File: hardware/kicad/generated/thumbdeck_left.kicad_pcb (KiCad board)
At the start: 2 copper layers, 63 x 107.9 mm, 0 parts

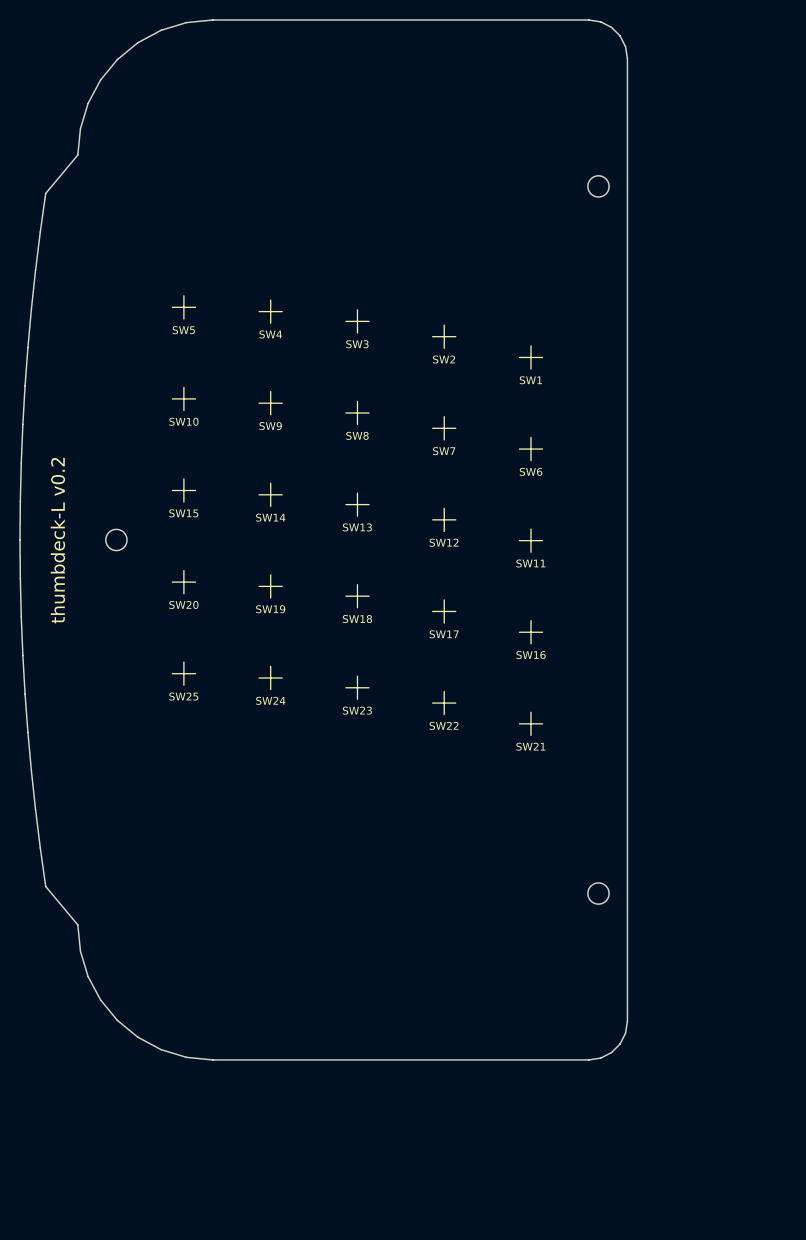
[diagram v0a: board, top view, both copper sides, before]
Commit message: hardware(v0.3): role-based geometry, grader, board gen
- deck.py: right grip = mcu (nice!nano/LiPo/USB-C/bridge), left = passive matrix
  + bridge connector; symmetric outline, mirrored key field
- grade.py: 17 checks incl. F-bridge + F-role; nice!nano pro_micro pin validity;
  single 5x10 transform (dropped split-specific checks)
- gen_kicad/render_fab/matrix_map updated for single controller

Co-Authored-By: Claude Opus 4.8 (1M context) <noreply@anthropic.com>
Claude-Session: https://claude.ai/code/session_01AmPvvwwHX98PjdDnPxhX97
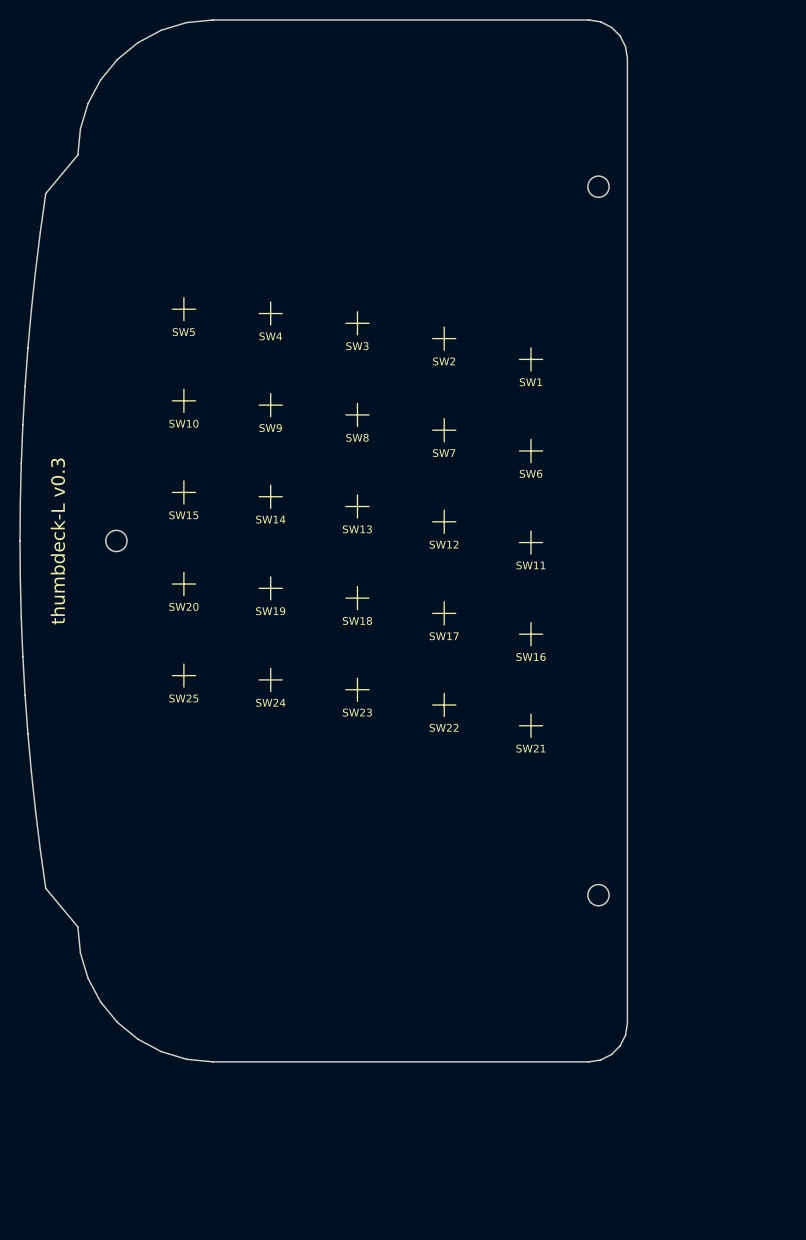
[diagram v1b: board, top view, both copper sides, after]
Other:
- board size 63 x 107.9 mm -> 63 x 108.1 mm
- board text added: "BRIDGE"
- board text added: "thumbdeck-L v0.3"
- board text removed: "CONTROLLER"
- board text removed: "LIPO"
- board text removed: "USB-C"
- board text removed: "thumbdeck-L v0.2"

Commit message: v0.4: encode EE design review into the grade, re-converge to PASS
Turn the professional EE review findings into enforced checks and fix the design
to satisfy them (functional 27/27, visual 9/9, OVERALL PASS).

Geometry/RF:
- nice!nano remounted vertical at top; nRF52840 ANTENNA keep-out overhangs the
  top edge (no copper under RF path), LiPo kept ~90mm away; USB in an access gap
- new hard check F-antenna; F-role now requires antenna on right / passive left

Bridge signal integrity:
- kscan debounce 8ms (F-si-debounce); BOM adds 4.7k row pull-downs, 100-330R
  column series R, TVS, shielded flex (F-si-passives, F-esd-tvs)

Process/plan gates (now graded):
- F-charge (1C vs cell), F-switch-verify (meter pinout), F-review-doc
  (docs/design-review.md + FMEA), F-bringup (current-draw checkpoints),
  F-fab-gates (README gates fab on schematic+ERC+DRC+CI)

Fixes: antenna/controller touching edge tripped float overlap -> 0.6mm gap;
BOM 'series res' substring broke on markdown bold -> looser check.
Bump VERSION v0.3 -> v0.4; regenerate all renders/board/soldermap.

Co-Authored-By: Claude Opus 4.8 (1M context) <noreply@anthropic.com>
Claude-Session: https://claude.ai/code/session_01AmPvvwwHX98PjdDnPxhX97
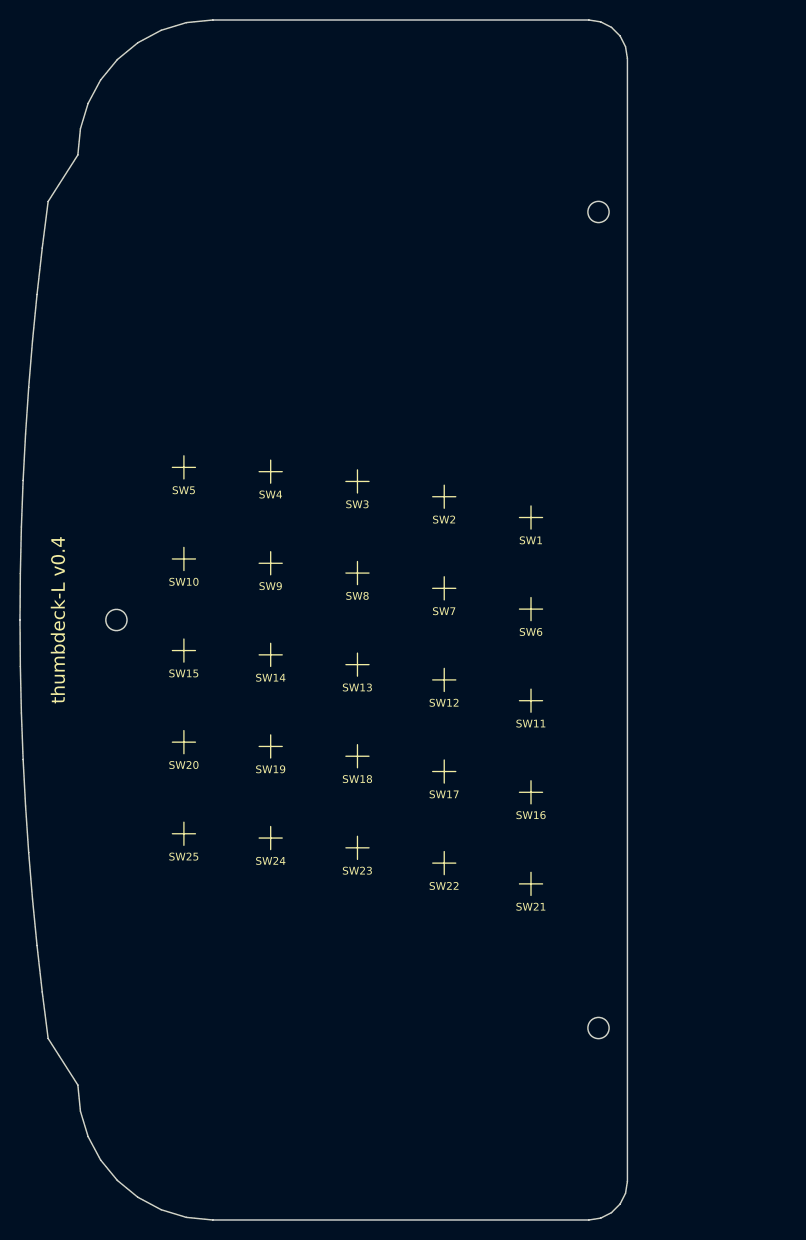
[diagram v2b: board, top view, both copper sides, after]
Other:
- board size 63 x 108.1 mm -> 63 x 124.5 mm
- board text added: "thumbdeck-L v0.4"
- board text removed: "thumbdeck-L v0.3"

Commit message: v0.12: snap-dome phone MagSafe deck — module, turnkey PCBA, stackable layer renders
Redesign from v0.4 (50-key nice!nano) to a landscape-phone MagSafe deck:

- Switches: Snaptron 7mm snap domes on a one-piece 3D-printed living-hinge keymat
  (PocketMage-style); footprint extracted to hardware/footprints/. 81 keys (2x 6x6
  grids + D-pad/OK + mouse + PgUp/Dn), digitized from the sketch to
  hardware/layout/keymat.json.
- Form: phone landscape, MagSafe-mounted centre; LiPo in the spine behind the ring;
  two ~70x102mm grips clamped to the outline; PCB-integrated trackpad (Azoteq IQS7211E).
- Electronics (5-lens EE/PD review): one Ebyte E73 nRF52840 module, 9x10 col2row
  matrix with SOD-323 diodes on the back, power front-end (MCP73831/USB-C+CC/ESD),
  vertical JST-GH bridge, ENIG. Layer-correct traces (cols front / rows back / vias),
  PCB meander antenna option.
- Sourcing (JLC vs PCBWay review): JLCPCB single-sided turnkey, ~$150-230/5 sets;
  part swaps + LCSC part numbers in docs/fabrication-sourcing.md.
- Real netlisted KiCad boards via pcbnew (gen_kicad_pcbnew.py) + front/back SVGs.
- 5 stackable layer renders (render_layers.py) + product/fab views; README rewritten.
- Cleanup: old 50-key loop scripts -> hardware/scripts/legacy/; old iters/renders
  -> renders/history/.

Co-Authored-By: Claude Opus 4.8 <noreply@anthropic.com>
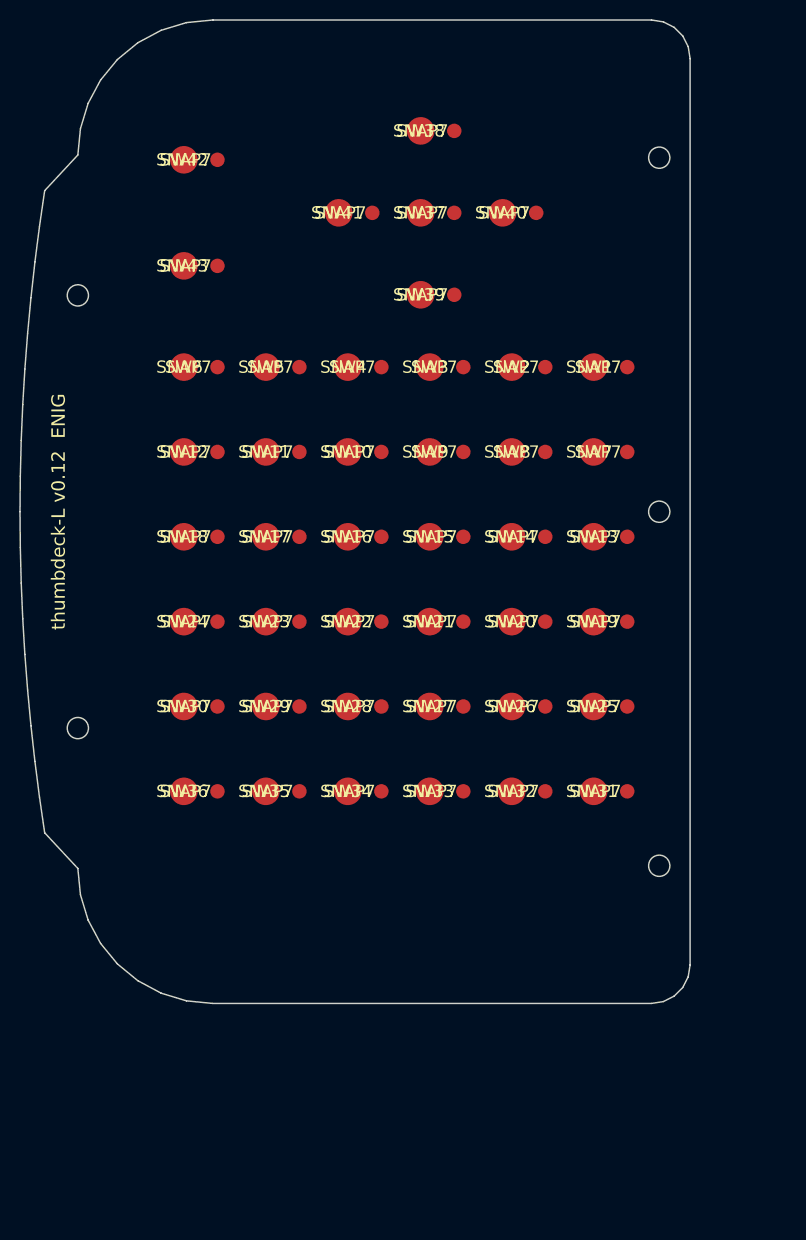
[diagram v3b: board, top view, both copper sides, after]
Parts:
- added D1: 1N4148WS, D_SOD-323, B.Cu at (59.5, 35.8)
- added D10: 1N4148WS, D_SOD-323, B.Cu at (34.0, 44.6)
- added D11: 1N4148WS, D_SOD-323, B.Cu at (25.5, 44.6)
- added D12: 1N4148WS, D_SOD-323, B.Cu at (17.0, 44.6)
- added D13: 1N4148WS, D_SOD-323, B.Cu at (59.5, 53.4)
- added D14: 1N4148WS, D_SOD-323, B.Cu at (51.0, 53.4)
- added D15: 1N4148WS, D_SOD-323, B.Cu at (42.5, 53.4)
- added D16: 1N4148WS, D_SOD-323, B.Cu at (34.0, 53.4)
- added D17: 1N4148WS, D_SOD-323, B.Cu at (25.5, 53.4)
- added D18: 1N4148WS, D_SOD-323, B.Cu at (17.0, 53.4)
- added D19: 1N4148WS, D_SOD-323, B.Cu at (59.5, 62.2)
- added D2: 1N4148WS, D_SOD-323, B.Cu at (51.0, 35.8)
- added D20: 1N4148WS, D_SOD-323, B.Cu at (51.0, 62.2)
- added D21: 1N4148WS, D_SOD-323, B.Cu at (42.5, 62.2)
- added D22: 1N4148WS, D_SOD-323, B.Cu at (34.0, 62.2)
- added D23: 1N4148WS, D_SOD-323, B.Cu at (25.5, 62.2)
- added D24: 1N4148WS, D_SOD-323, B.Cu at (17.0, 62.2)
- added D25: 1N4148WS, D_SOD-323, B.Cu at (59.5, 71.0)
- added D26: 1N4148WS, D_SOD-323, B.Cu at (51.0, 71.0)
- added D27: 1N4148WS, D_SOD-323, B.Cu at (42.5, 71.0)
- added D28: 1N4148WS, D_SOD-323, B.Cu at (34.0, 71.0)
- added D29: 1N4148WS, D_SOD-323, B.Cu at (25.5, 71.0)
- added D3: 1N4148WS, D_SOD-323, B.Cu at (42.5, 35.8)
- added D30: 1N4148WS, D_SOD-323, B.Cu at (17.0, 71.0)
- added D31: 1N4148WS, D_SOD-323, B.Cu at (59.5, 79.8)
- added D32: 1N4148WS, D_SOD-323, B.Cu at (51.0, 79.8)
- added D33: 1N4148WS, D_SOD-323, B.Cu at (42.5, 79.8)
- added D34: 1N4148WS, D_SOD-323, B.Cu at (34.0, 79.8)
- added D35: 1N4148WS, D_SOD-323, B.Cu at (25.5, 79.8)
- added D36: 1N4148WS, D_SOD-323, B.Cu at (17.0, 79.8)
- added D37: 1N4148WS, D_SOD-323, B.Cu at (41.6, 19.8)
- added D38: 1N4148WS, D_SOD-323, B.Cu at (41.6, 11.3)
- added D39: 1N4148WS, D_SOD-323, B.Cu at (41.6, 28.3)
- added D4: 1N4148WS, D_SOD-323, B.Cu at (34.0, 35.8)
- added D40: 1N4148WS, D_SOD-323, B.Cu at (50.1, 19.8)
- added D41: 1N4148WS, D_SOD-323, B.Cu at (33.1, 19.8)
- added D42: 1N4148WS, D_SOD-323, B.Cu at (17.0, 14.3)
- added D43: 1N4148WS, D_SOD-323, B.Cu at (17.0, 25.3)
- added D5: 1N4148WS, D_SOD-323, B.Cu at (25.5, 35.8)
- added D6: 1N4148WS, D_SOD-323, B.Cu at (17.0, 35.8)
- added D7: 1N4148WS, D_SOD-323, B.Cu at (59.5, 44.6)
- added D8: 1N4148WS, D_SOD-323, B.Cu at (51.0, 44.6)
- added D9: 1N4148WS, D_SOD-323, B.Cu at (42.5, 44.6)
- added SW1: SNAP7, , F.Cu at (59.5, 36.0)
- added SW10: SNAP7, , F.Cu at (34.0, 44.8)
- added SW11: SNAP7, , F.Cu at (25.5, 44.8)
- added SW12: SNAP7, , F.Cu at (17.0, 44.8)
- added SW13: SNAP7, , F.Cu at (59.5, 53.6)
- added SW14: SNAP7, , F.Cu at (51.0, 53.6)
- added SW15: SNAP7, , F.Cu at (42.5, 53.6)
- added SW16: SNAP7, , F.Cu at (34.0, 53.6)
- added SW17: SNAP7, , F.Cu at (25.5, 53.6)
- added SW18: SNAP7, , F.Cu at (17.0, 53.6)
- added SW19: SNAP7, , F.Cu at (59.5, 62.4)
- added SW2: SNAP7, , F.Cu at (51.0, 36.0)
- added SW20: SNAP7, , F.Cu at (51.0, 62.4)
- added SW21: SNAP7, , F.Cu at (42.5, 62.4)
- added SW22: SNAP7, , F.Cu at (34.0, 62.4)
- added SW23: SNAP7, , F.Cu at (25.5, 62.4)
- added SW24: SNAP7, , F.Cu at (17.0, 62.4)
- added SW25: SNAP7, , F.Cu at (59.5, 71.2)
- added SW26: SNAP7, , F.Cu at (51.0, 71.2)
- added SW27: SNAP7, , F.Cu at (42.5, 71.2)
- added SW28: SNAP7, , F.Cu at (34.0, 71.2)
- added SW29: SNAP7, , F.Cu at (25.5, 71.2)
- added SW3: SNAP7, , F.Cu at (42.5, 36.0)
- added SW30: SNAP7, , F.Cu at (17.0, 71.2)
- added SW31: SNAP7, , F.Cu at (59.5, 80.0)
- added SW32: SNAP7, , F.Cu at (51.0, 80.0)
- added SW33: SNAP7, , F.Cu at (42.5, 80.0)
- added SW34: SNAP7, , F.Cu at (34.0, 80.0)
- added SW35: SNAP7, , F.Cu at (25.5, 80.0)
- added SW36: SNAP7, , F.Cu at (17.0, 80.0)
- added SW37: SNAP7, , F.Cu at (41.6, 20.0)
- added SW38: SNAP7, , F.Cu at (41.6, 11.5)
- added SW39: SNAP7, , F.Cu at (41.6, 28.5)
- added SW4: SNAP7, , F.Cu at (34.0, 36.0)
- added SW40: SNAP7, , F.Cu at (50.1, 20.0)
- added SW41: SNAP7, , F.Cu at (33.1, 20.0)
- added SW42: SNAP7, , F.Cu at (17.0, 14.5)
- added SW43: SNAP7, , F.Cu at (17.0, 25.5)
- added SW5: SNAP7, , F.Cu at (25.5, 36.0)
- added SW6: SNAP7, , F.Cu at (17.0, 36.0)
- added SW7: SNAP7, , F.Cu at (59.5, 44.8)
- added SW8: SNAP7, , F.Cu at (51.0, 44.8)
- added SW9: SNAP7, , F.Cu at (42.5, 44.8)
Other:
- board size 63 x 124.5 mm -> 69.5 x 102 mm
- board text added: "ROUTING + MODULE/CONN FOOTPRINTS = NEXT GATE"
- board text added: "thumbdeck-L v0.12 ENIG"
- board text removed: "D1"
- board text removed: "D10"
- board text removed: "D11"
- board text removed: "D12"
- board text removed: "D13"
- board text removed: "D14"
- board text removed: "D15"
- board text removed: "D16"
- board text removed: "D17"
- board text removed: "D18"
- board text removed: "D19"
- board text removed: "D2"
- board text removed: "D20"
- board text removed: "D21"
- board text removed: "D22"
- board text removed: "D23"
- board text removed: "D24"
- board text removed: "D25"
- board text removed: "D3"
- board text removed: "D4"
- board text removed: "D5"
- board text removed: "D6"
- board text removed: "D7"
- board text removed: "D8"
- board text removed: "D9"
- board text removed: "SW1"
- board text removed: "SW10"
- board text removed: "SW11"
- board text removed: "SW12"
- board text removed: "SW13"
- board text removed: "SW14"
- board text removed: "SW15"
- board text removed: "SW16"
- board text removed: "SW17"
- board text removed: "SW18"
- board text removed: "SW19"
- board text removed: "SW2"
- board text removed: "SW20"
- board text removed: "SW21"
- board text removed: "SW22"
- board text removed: "SW23"
- board text removed: "SW24"
- board text removed: "SW25"
- board text removed: "SW3"
- board text removed: "SW4"
- board text removed: "SW5"
- board text removed: "SW6"
- board text removed: "SW7"
- board text removed: "SW8"
- board text removed: "SW9"
- board text removed: "SWITCH FOOTPRINT PROVISIONAL - VERIFY vs DATASHEET"
- board text removed: "thumbdeck-L v0.4"

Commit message: v0.13: printable pitch, 2u space bar, cluster/screw/keymat fixes
Feedback fixes (all verified: no overlaps, nothing off-board, no screw in a keep-out):
- #5 DFM: pitch 8.5/8.8 -> 9.5mm so the inter-key wall is ~1.5mm (printable in PETG;
  0.5mm was not). Matches the i8+ pitch. Grips -> 74.5x109.5mm, 79 keys.
- #4: drop MENU keys, shift bottom row, add a double-wide 2u space bar per side
  (dome stays single under the wide keycap; keys carry a 'w' width in units).
- #2: D-pad no longer overlaps the F-row (upper zone sized to clear the cluster,
  clusters centred instead of offset down).
- #1: bottom-inner mount hole moved below the vertical JST-GH bridge connector.
- #3: keymat now ties every cluster keycap into the living-hinge web.

Co-Authored-By: Claude Opus 4.8 <noreply@anthropic.com>
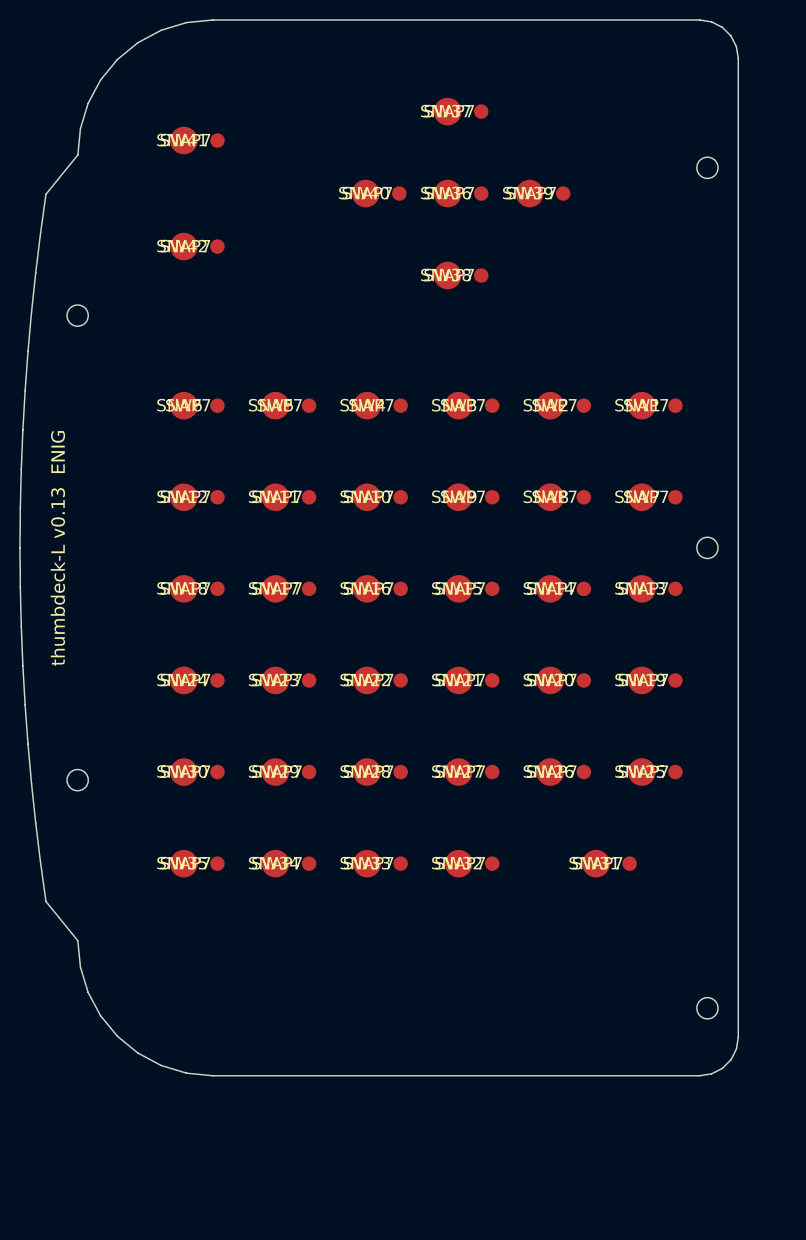
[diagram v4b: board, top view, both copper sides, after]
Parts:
- removed D43: 1N4148WS, D_SOD-323
- removed SW43: SNAP7, 
- moved D36 67.8 mm to (44.4, 17.8)
- moved SW36 67.8 mm to (44.4, 18.0)
- moved D41 17.7 mm to (17.0, 12.3)
- moved SW41 17.7 mm to (17.0, 12.5)
- moved D39 15.4 mm to (52.9, 17.8)
- moved SW39 15.4 mm to (52.9, 18.0)
- moved D38 15.3 mm to (44.4, 26.3)
- moved SW38 15.3 mm to (44.4, 26.5)
- moved D40 14.3 mm to (35.9, 17.8)
- moved SW40 14.3 mm to (35.9, 18.0)
- moved D35 11.3 mm to (17.0, 87.3)
- moved SW35 11.3 mm to (17.0, 87.5)
- moved D37 10.9 mm to (44.4, 9.30)
- moved SW37 10.9 mm to (44.4, 9.50)
- moved D34 10.6 mm to (26.5, 87.3)
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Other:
- board size 69.5 x 102 mm -> 74.5 x 109.5 mm
- board text added: "thumbdeck-L v0.13 ENIG"
- board text removed: "thumbdeck-L v0.12 ENIG"
